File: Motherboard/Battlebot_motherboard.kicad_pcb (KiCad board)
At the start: 2 copper layers, 42 x 61.5 mm, 30 parts

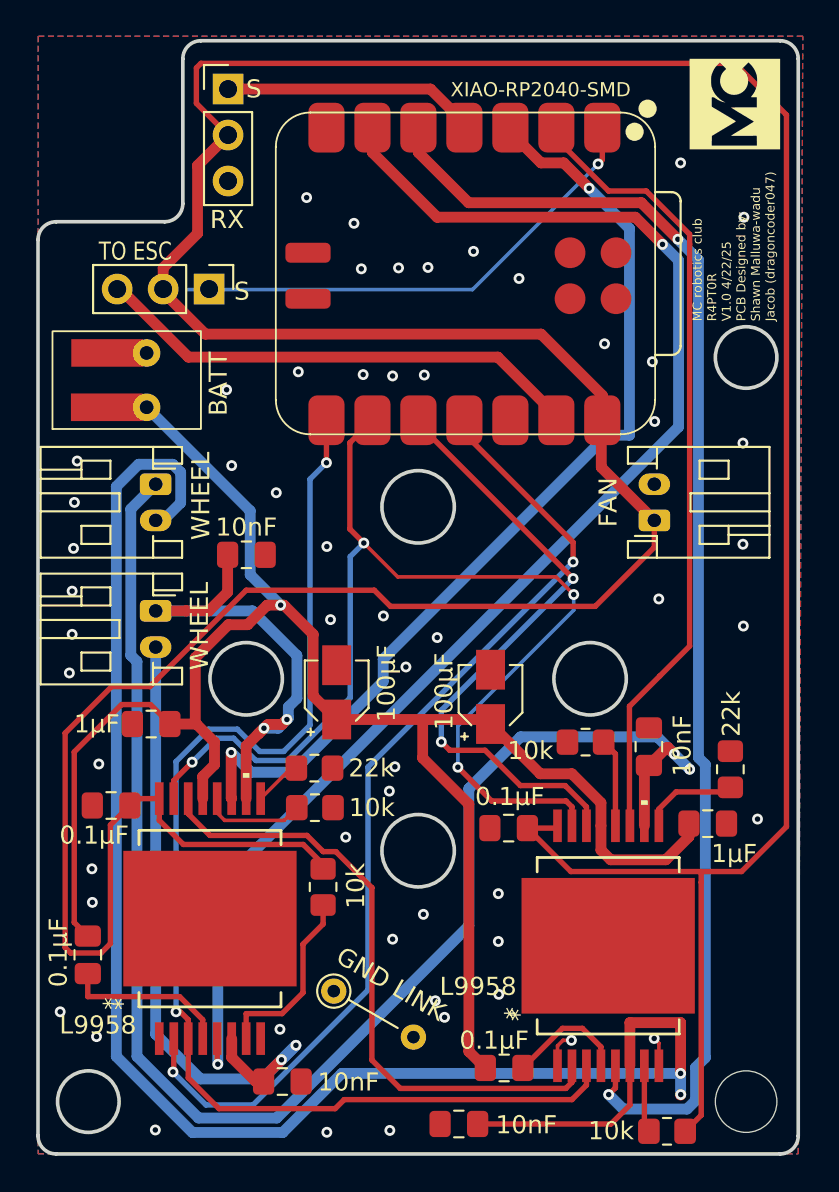
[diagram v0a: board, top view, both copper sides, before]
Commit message: change width of a few tracks
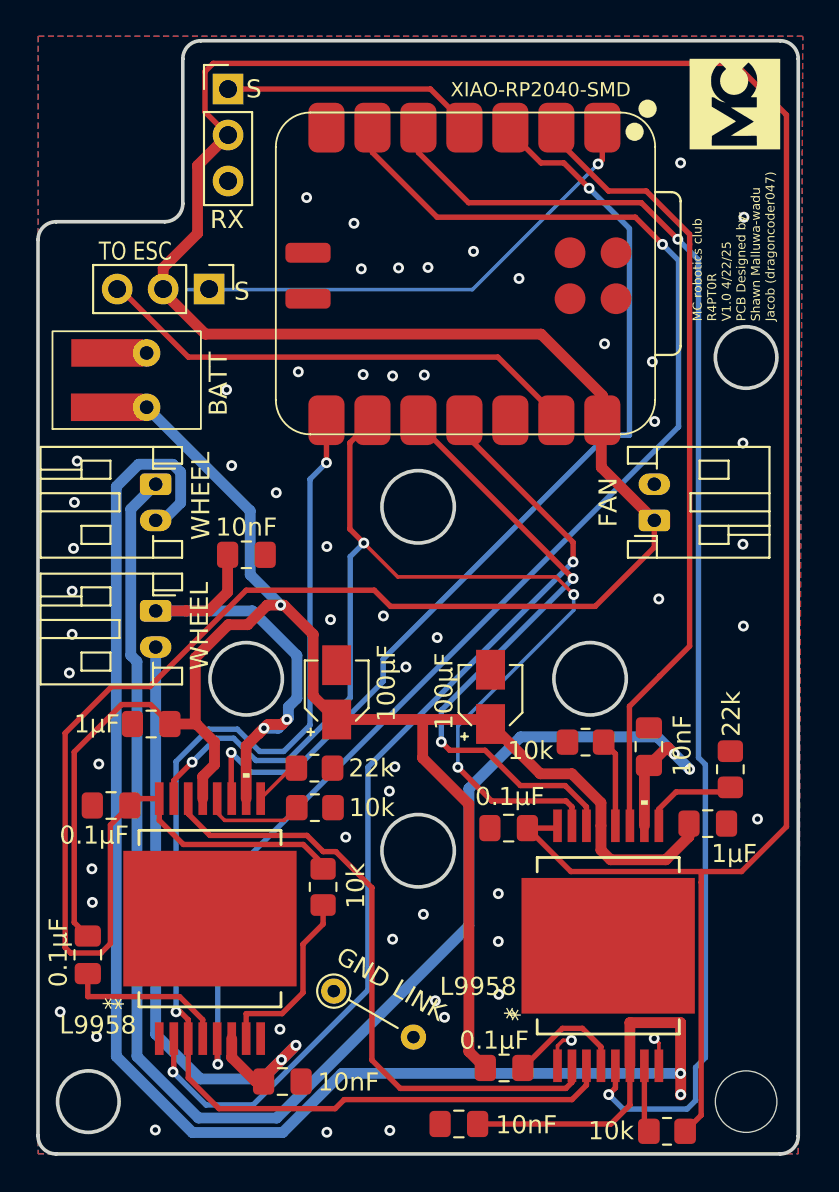
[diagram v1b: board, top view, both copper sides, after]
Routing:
- net +5V: track 230.9 -> 230.1 mm

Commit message: new cap footprint and rerouting for it
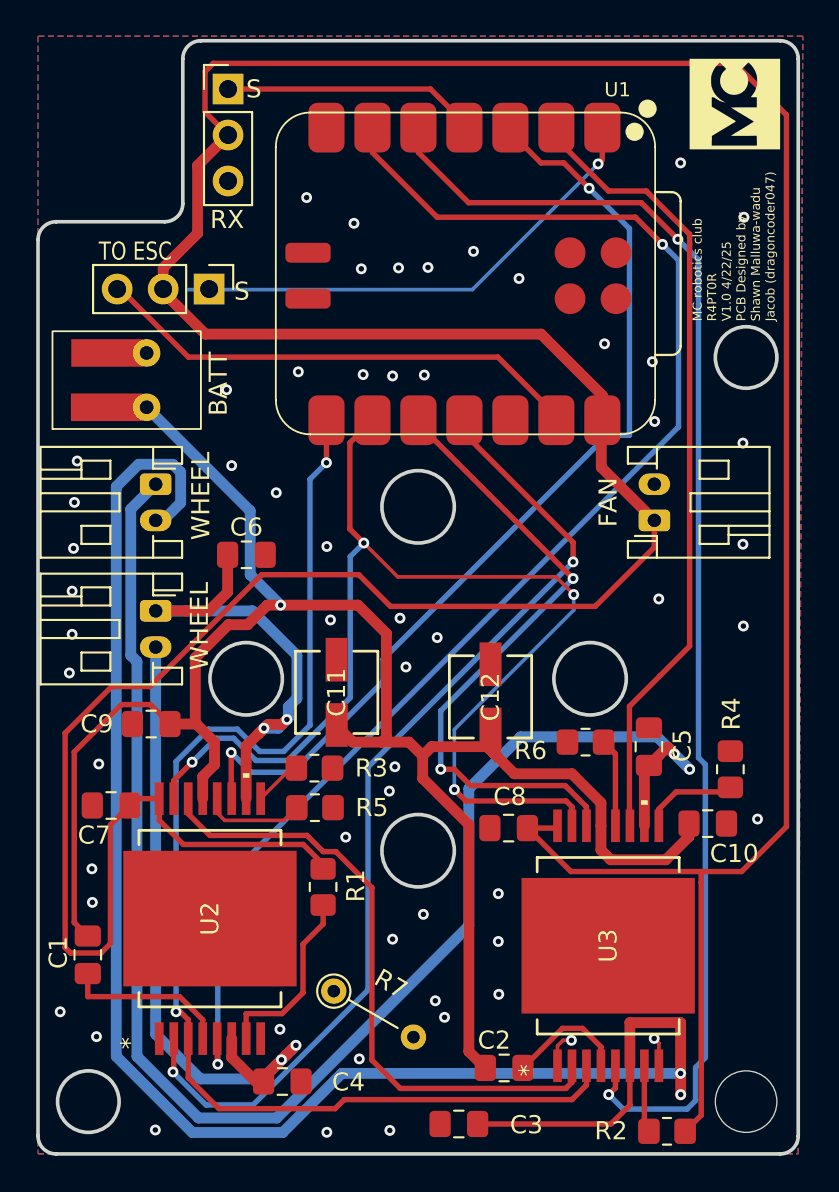
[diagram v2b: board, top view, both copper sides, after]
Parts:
- C11, C12: renamed from 100µF; footprint Capacitor_SMD:CP_Elec_3x5.3 -> footprints:CAP_UCD_4X5P8_NCH
- R7: renamed from GND LINK
- renumbered 0.1µF to C1, 1µF to C10, 0.1µF to C2, 10nF to C3, 10nF to C4, 10nF to C5, 10nF to C6, 0.1µF to C7, 0.1µF to C8, 1µF to C9, 10k to R1, 10k to R2, 22k to R3, 22k to R4, 10k to R5, 10k to R6, XIAO-RP2040-SMD to U1, L9958 to U2, L9958 to U3
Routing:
- net +12V: track 102.0 -> 107.3 mm
- net SCK: track 63.4 -> 64.4 mm
- net µSO: track 34.9 -> 35.8 mm
- net +5V: track 230.1 -> 230.8 mm
- net GND: vias 56 -> 57

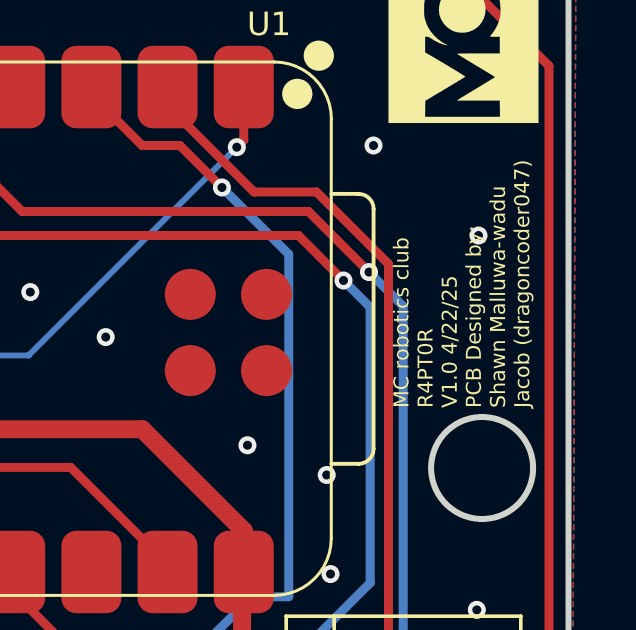
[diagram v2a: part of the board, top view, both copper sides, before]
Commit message: updated silkscreen
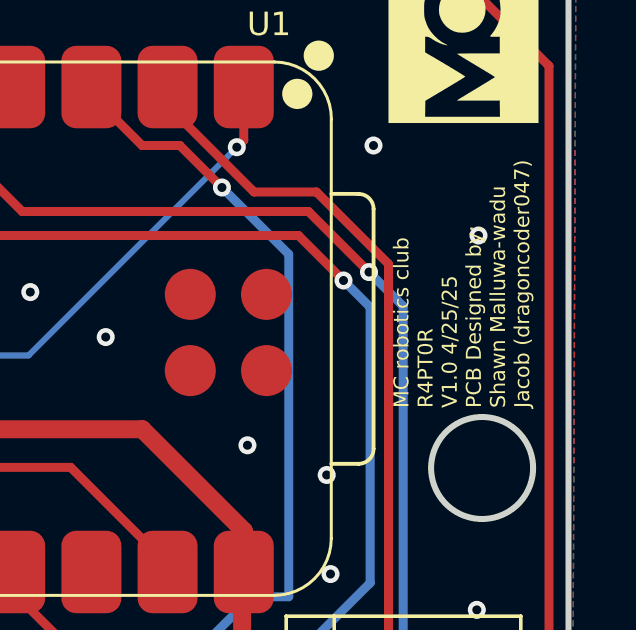
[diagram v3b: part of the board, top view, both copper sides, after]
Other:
- board text added: "MC robotics club R4PT0R V1.0 4/25/25 PCB Designed by: Shawn Malluwa-wadu Jacob (dragoncoder047)"
- board text removed: "MC robotics club R4PT0R V1.0 4/22/25 PCB Designed by: Shawn Malluwa-wadu Jacob (dragoncoder047)"
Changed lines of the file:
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@@
 		)
 	)
-	(gr_text "MC robotics club\nR4PT0R\nV1.0 4/22/25\nPCB Designed by:\nShawn Malluwa-wadu\nJacob (dragoncoder047)"
+	(gr_text "MC robotics club\nR4PT0R\nV1.0 4/25/25\nPCB Designed by:\nShawn Malluwa-wadu\nJacob (dragoncoder047)"
 		(at 188.75 57 90)
 		(layer "F.SilkS")

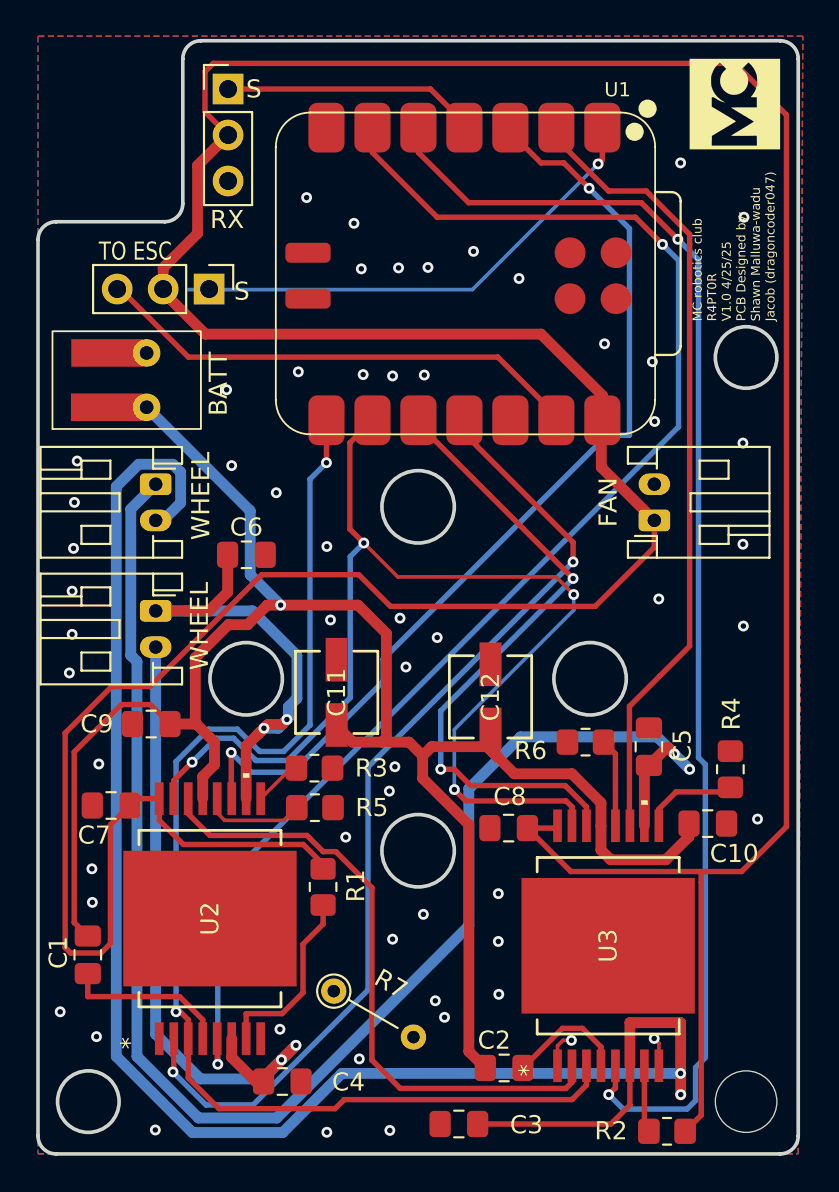
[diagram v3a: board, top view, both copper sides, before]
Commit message: update with rounded tracks
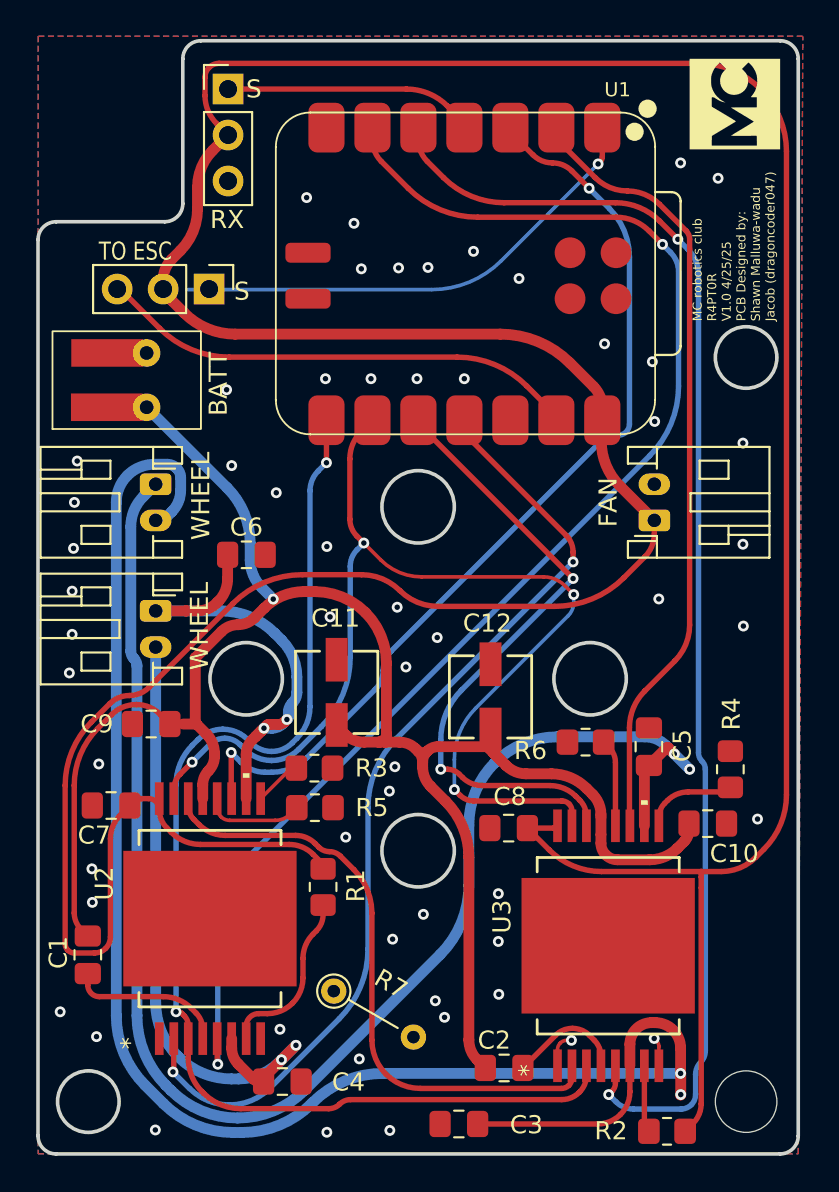
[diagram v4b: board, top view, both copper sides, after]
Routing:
- net +5V: track 230.8 -> 225.6 mm
- net Net-(J5-Pin_2): track 93.7 -> 90.9 mm
- net Net-(J5-Pin_1): track 83.6 -> 81.8 mm
- net SCK: track 64.4 -> 62.9 mm
- net CS: track 68.7 -> 67.5 mm
- net PWM2: track 53.9 -> 52.8 mm
- net DIR2: track 77.1 -> 76.1 mm
- net µSI: track 54.8 -> 53.7 mm
- net DIR1: track 73.2 -> 72.3 mm
- net 1SO: track 35.0 -> 34.2 mm
- net Net-(J6-Pin_2): track 37.0 -> 36.3 mm
- net +12V: track 107.3 -> 106.6 mm
- net Net-(U2-DI): track 10.3 -> 9.64 mm
- net PWM1: track 44.2 -> 43.6 mm
- net Net-(J4-Pin_3): track 27.2 -> 26.7 mm
